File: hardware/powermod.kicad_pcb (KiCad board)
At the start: 4 copper layers, 65 x 40 mm, 77 parts, among them J1 USB_C_IN, J2 USB_C_OUT, J3 JST_PH_2, J4 STEMMA_QT, J5 SWD_HDR, Q1 AON7407, Q2 AON7407, Q3 BSS138, SW1 BUTTON, U1 BM8563, U2 PY32F003F18P6, U3 TPS63020DSJR, U4 TP4056, U5 XC6206P332MR, Y1 32.768kHz

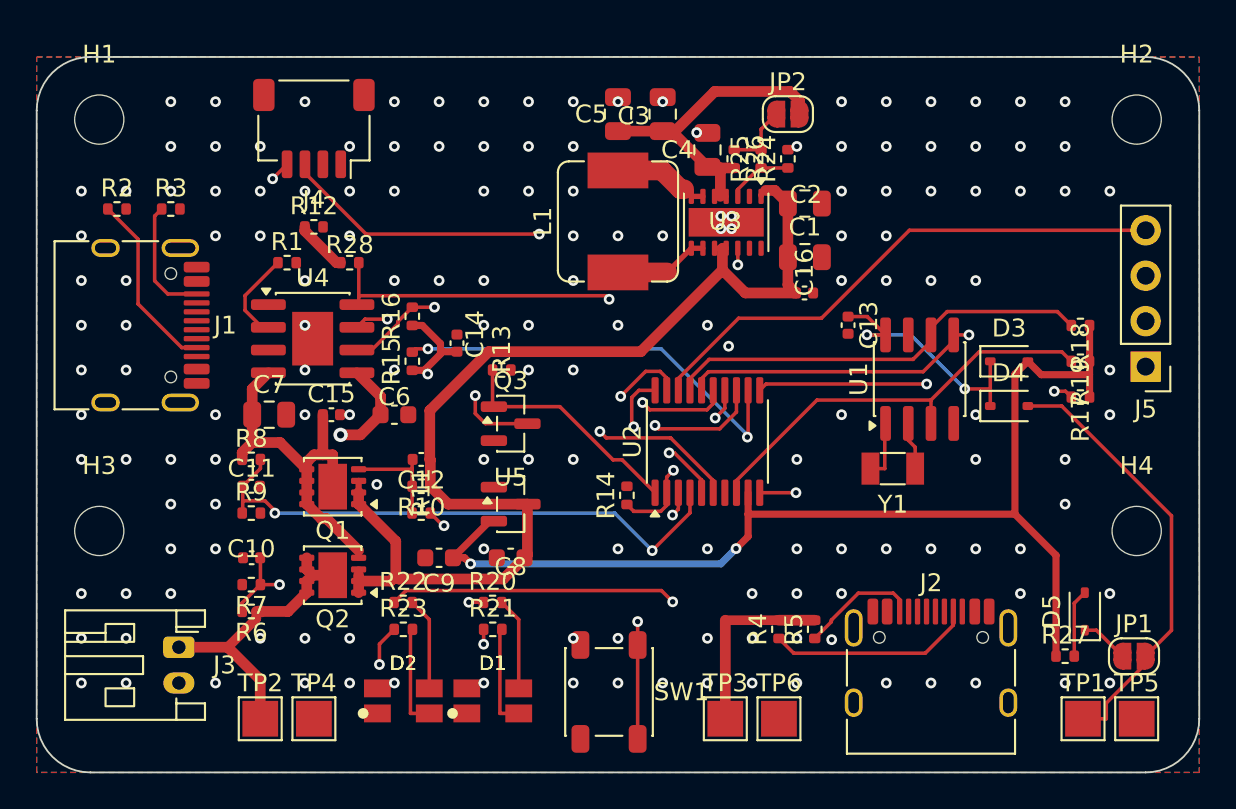
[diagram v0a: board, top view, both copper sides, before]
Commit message: hardware: full reroute (component tweak) - VOUT trunk now routed
The latest tweak opened the VOUT lane: the U3->J2 distribution trunk routes
cleanly this run (the 23mm gap from f555fb9 is gone). EP re-cleaned (4 tented
GND ties, 0 foreign vias), CC on A8/B8, pad-diff 226/226. 419 tracks, 201 vias.

DRC: 4 track_width (L1N/L2 default-width, to re-widen) + 6 unconnected. The
unconnected are the 4 fine-pitch escapes (J1.A4/A9 VBUS, J2.A4/A9 VOUT) plus
TP3.1 - a VOUT test point placed 14mm from any VOUT copper at the board's
bottom-left; the router can't reach it through the mid-board congestion.

Co-Authored-By: Claude Opus 4.8 <noreply@anthropic.com>
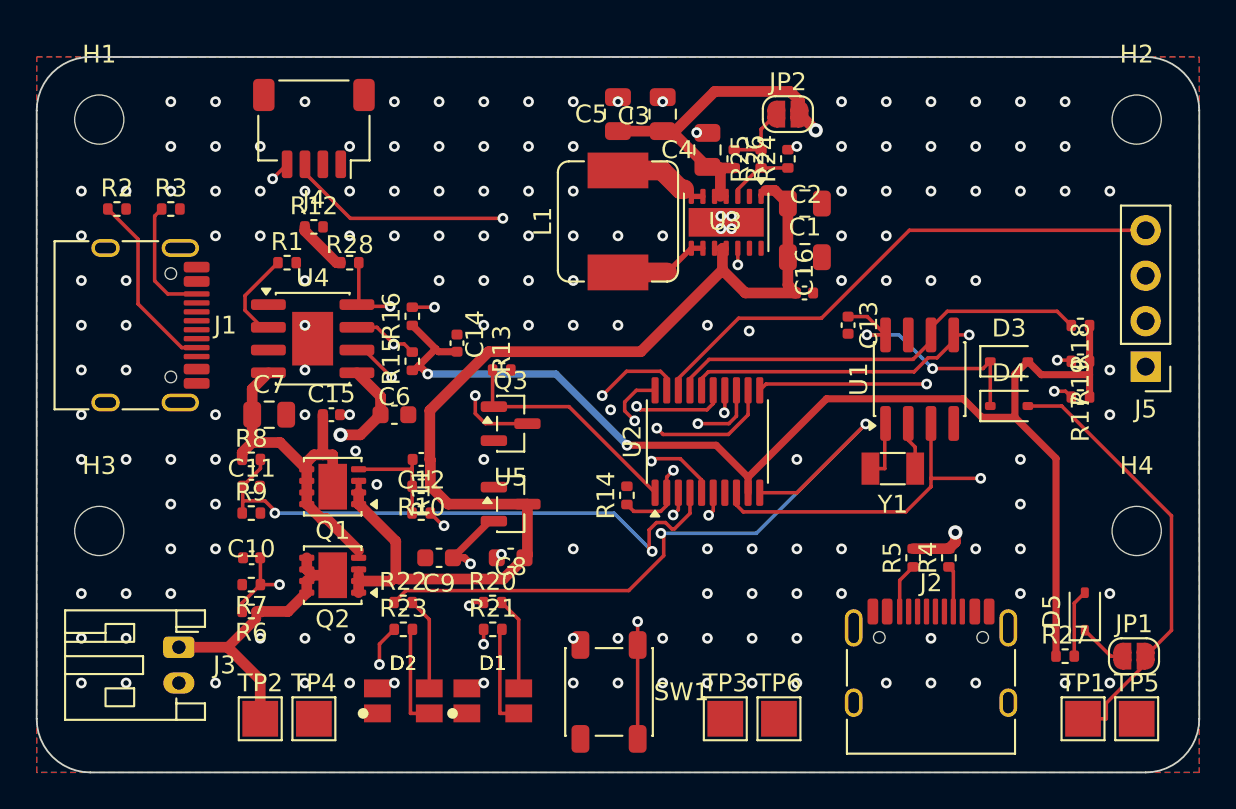
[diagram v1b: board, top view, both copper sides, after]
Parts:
- moved R4 10.3 mm to (51.0, 28.0)
- moved R5 6.80 mm to (49.0, 28.0)
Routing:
- net VOUT: track 29.1 -> 48.6 mm, vias 0 -> 2
- net CHG_STDBY: track 25.7 -> 37.3 mm, vias 2 -> 3
- net CC1_OUT: track 11.5 -> 2.60 mm
- net LED_BAT_B: track 63.3 -> 71.8 mm
- net SDA: track 38.9 -> 30.8 mm
- net LED_BAT_A: track 52.8 -> 58.4 mm
- net CHG_CHRG: track 28.4 -> 33.3 mm, vias 3 -> 2
- net 3V3: track 80.8 -> 85.5 mm
- net RTC_INT: track 23.9 -> 28.3 mm, vias 0 -> 2
- net CC2_OUT: track 6.67 -> 2.81 mm
- net VBUS_DIV: track 31.7 -> 32.9 mm
- net CHG_CE: track 29.8 -> 28.6 mm
- net SCL: track 35.3 -> 34.4 mm
- net LED_PWR_A: track 19.8 -> 20.7 mm
- net GND: vias 159 -> 160

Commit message: hardware: CORRECT USB-C CC pins -> A5/B5 (revert a2826a7) + full reroute
Deep pre-fab audit found the USB-C CC assignment was WRONG: a2826a7 moved CC to
A8/B8 (the SBU pins) on a false "mirrored footprint" claim. Verified 3 ways that
A5=CC1/B5=CC2 and A8/B8=SBU: (1) USB-C spec; (2) real C165948 = TYPE-C-31-M-12
standard pinout (LCSC/EasyEDA land pattern); (3) KiCad's HRO TYPE-C-31-M-12
footprint is geometrically identical to ours (A5@-1.25=CC1, A8@+1.25=SBU1). With
CC on A8/B8 the Rp/Rd resistors sat on floating SBU pins -> board would never
negotiate VBUS.

Fix: netlist CC back to A5/B5, A8/B8->NC. R4/R5 CC labels swapped (symmetric 56k)
so each Rp stays beside its pad after the move. Board pads reassigned to match;
full Freerouting reroute. pad-diff 226/226, CC verified on A5/B5, DRC 0 shorts.

Remaining hand-finish (this seed): 4 track_width (L1N/L2 necks), and unrouted =
J1/J2 VBUS/VOUT escapes + CC2_IN(B5) + R5.2(VOUT) + TP3. EP got 1 GND tie this
run (In2 SCL crowds it).

Co-Authored-By: Claude Opus 4.8 <noreply@anthropic.com>
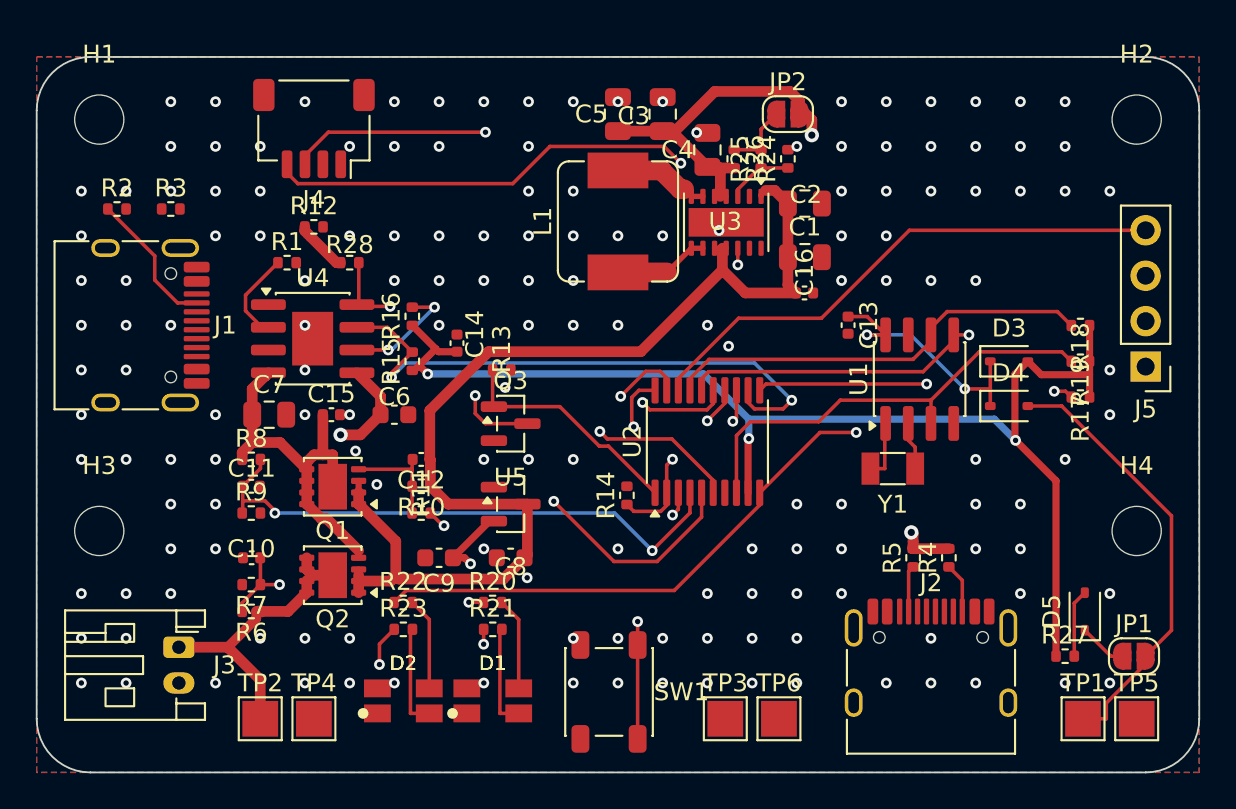
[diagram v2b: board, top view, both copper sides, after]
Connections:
- J1 pad A5: (no net) -> CC1_IN
- J1 pad A8: CC1_IN -> (no net)
- J1 pad B5: (no net) -> CC2_IN
- J1 pad B8: CC2_IN -> (no net)
- J2 pad A5: (no net) -> CC1_OUT
- J2 pad A8: CC1_OUT -> (no net)
- J2 pad B5: (no net) -> CC2_OUT
- J2 pad B8: CC2_OUT -> (no net)
- R4 pad 1: CC1_OUT -> CC2_OUT
- R5 pad 1: CC2_OUT -> CC1_OUT
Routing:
- net CHG_STDBY: track 37.3 -> 26.9 mm
- net SDA: track 30.8 -> 40.3 mm
- net LED_BAT_A: track 58.4 -> 50.3 mm, vias 2 -> 1
- net SCL: track 34.4 -> 42.2 mm
- net CC2_IN: track 6.83 -> 0.00 mm
- net LED_BAT_B: track 71.8 -> 68.3 mm
- net RTC_INT: track 28.3 -> 25.4 mm, vias 2 -> 0
- net CHG_CE: track 28.6 -> 31.4 mm
- net CC1_IN: track 10.3 -> 7.93 mm
- net VBUS_DIV: track 32.9 -> 31.7 mm
- net LED_PWR_A: track 20.7 -> 19.8 mm
- net VOUT: track 48.6 -> 47.8 mm
- net CHG_CHRG: track 33.3 -> 32.6 mm
- net 3V3: track 85.5 -> 85.7 mm, vias 3 -> 4
- net GND: vias 160 -> 157

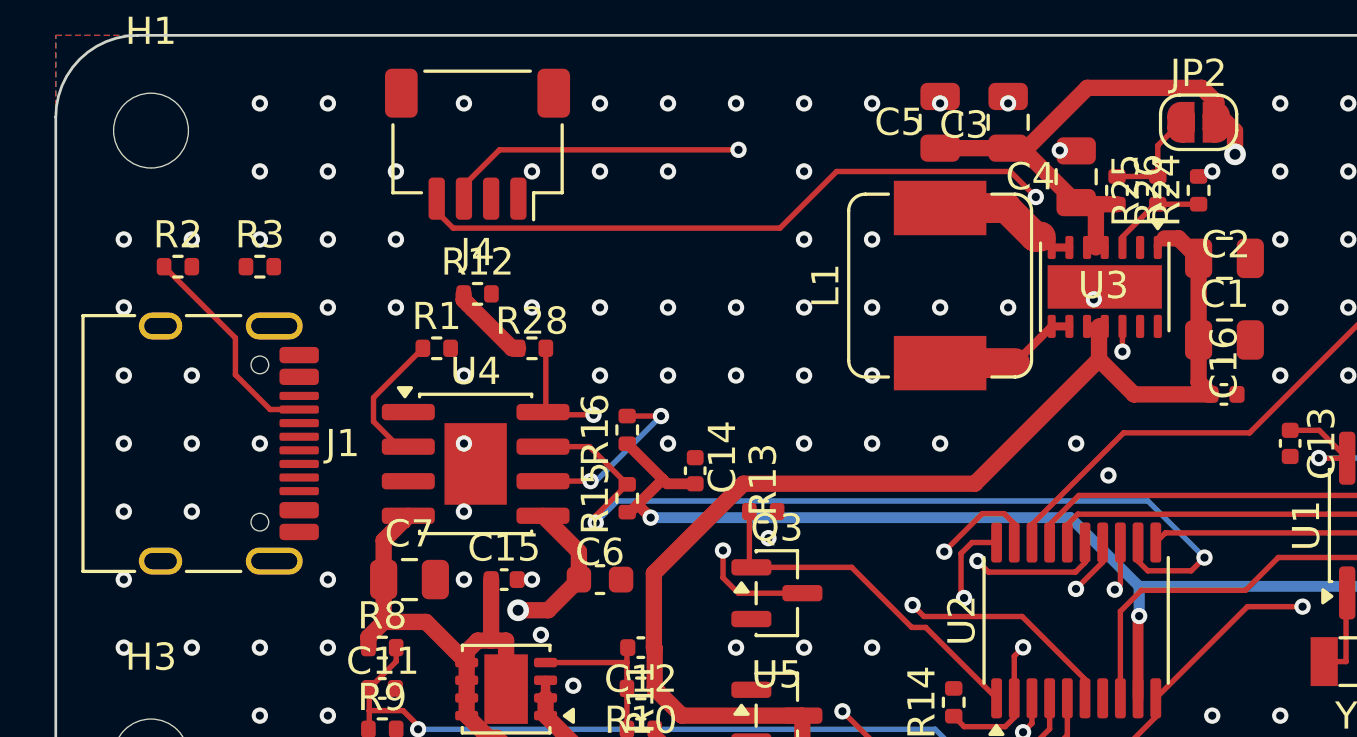
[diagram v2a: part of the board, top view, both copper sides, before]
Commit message: hardware: full reroute (component tweak) - CC fully routed to A5/B5
Re-ran after component tweaks. CC now FULLY routed to the correct A5/B5 pads
(both J1 and J2). pad-diff 226/226, 0 shorts/clearance. EP: 2 tented GND ties
(In2 routing crowds the EP this seed). 413 tracks.

DRC: 4 track_width (L1N/L2 necks) + 6 unconnected = J1/J2 VBUS/VOUT escapes,
R5.2 (VOUT stub islanded from main VOUT), TP3 (VOUT test point).

Co-Authored-By: Claude Opus 4.8 <noreply@anthropic.com>
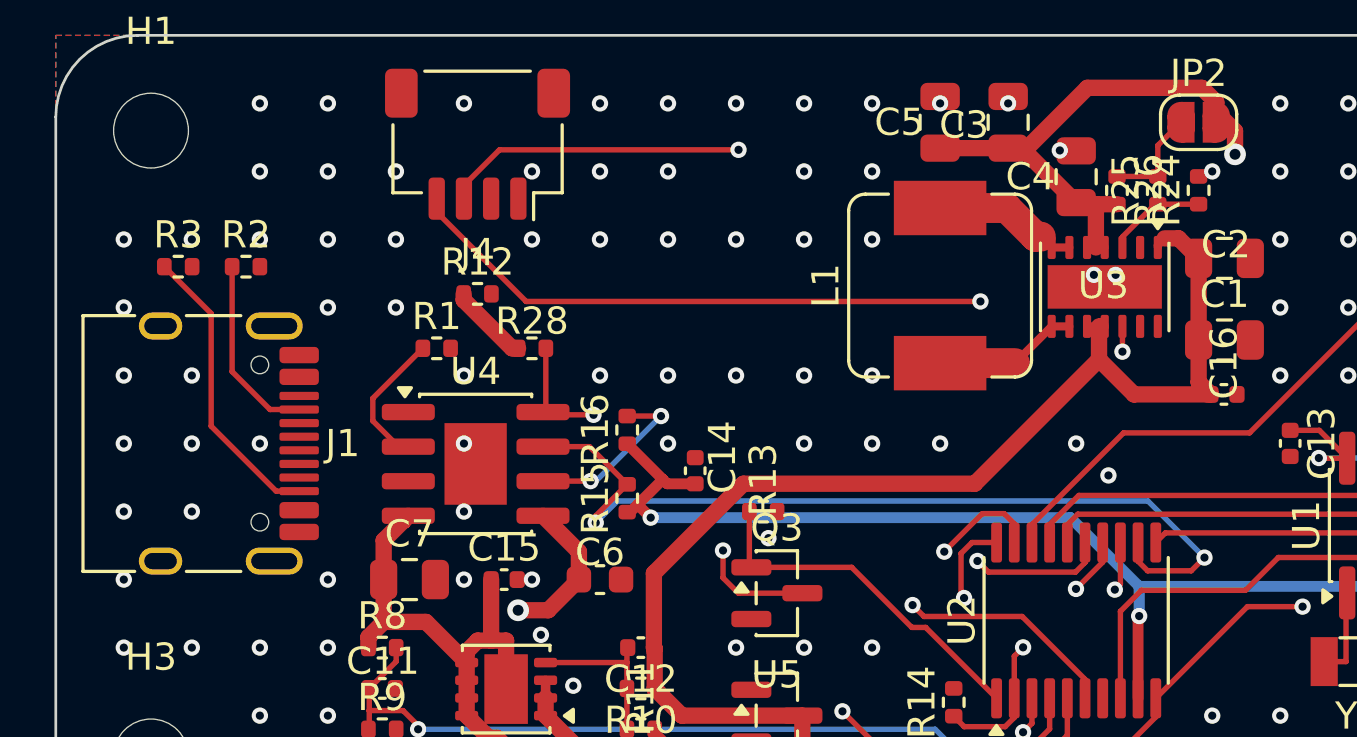
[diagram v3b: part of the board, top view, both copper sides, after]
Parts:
- moved R3 3.00 mm to (4.50, 8.50)
- moved R2 2.50 mm to (6.99, 8.50)
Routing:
- net CC2_IN: track 0.00 -> 10.8 mm
- net SCL: track 42.2 -> 39.6 mm
- net CC1_IN: track 7.93 -> 6.90 mm
- net GND: vias 157 -> 155
